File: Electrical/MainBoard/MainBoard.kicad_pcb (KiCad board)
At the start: 4 copper layers, 100 x 100 mm, 152 parts, among them J1 SNAP Program, J10 Refl_Mount, J11 Refl_Mount, J12 Refl_Mount, J13 Refl_PCB_Connect, J14 Refl_PCB_Connect, J15 Refl_PCB_Connect, J16 Conn_02x03_Odd_Even, J17 MEM2061-01-188-00-A, J18 Conn_02x02_Odd_Even, J19 Conn_02x03_Odd_Even, J2 3.3V Supply, J20 Conn_02x03_Odd_Even, J21 Conn_02x03_Odd_Even, J22 Conn_02x02_Odd_Even, J23 Conn_02x03_Odd_Even, J24 Conn_01x04, J3 5V Supply, J4 USB_B_Micro, J5 Battery1, J6 Battery1, J7 GPIO1, J8 Conn_02x04_Odd_Even, J9 USB_B_Micro, K1 QRE1113GR, K2 QRE1113GR, K3 QRE1113GR, M1 Motor_DC, M2 Motor_DC, SW1 Reset, SW10 SW_SPST, SW2 5V Bypass, SW3 All Power Switch, SW4 User_Button, SW5 User_Button, SW6 User_Button, SW7 SW_SPST, SW8 SW_SPST, SW9 SW_SPST, U1 PIC32MZ2048EFH144-I/PL, U10 DRV8842PWPR, U11 Quad_Encoder, U12 Quad_Encoder, U13 DRV8842PWPR, U15 M95M01-DFMN6TP, U2 AP2114HA-3.3TRG1, U3 AP2114HA-3.3TRG1, U4 ICM-42688-P, U5 GSF7002DW, U6 GSF7002DW, U7 GSF7002DW, U8 GSF7002DW, U9 MCP2221A-I_SL

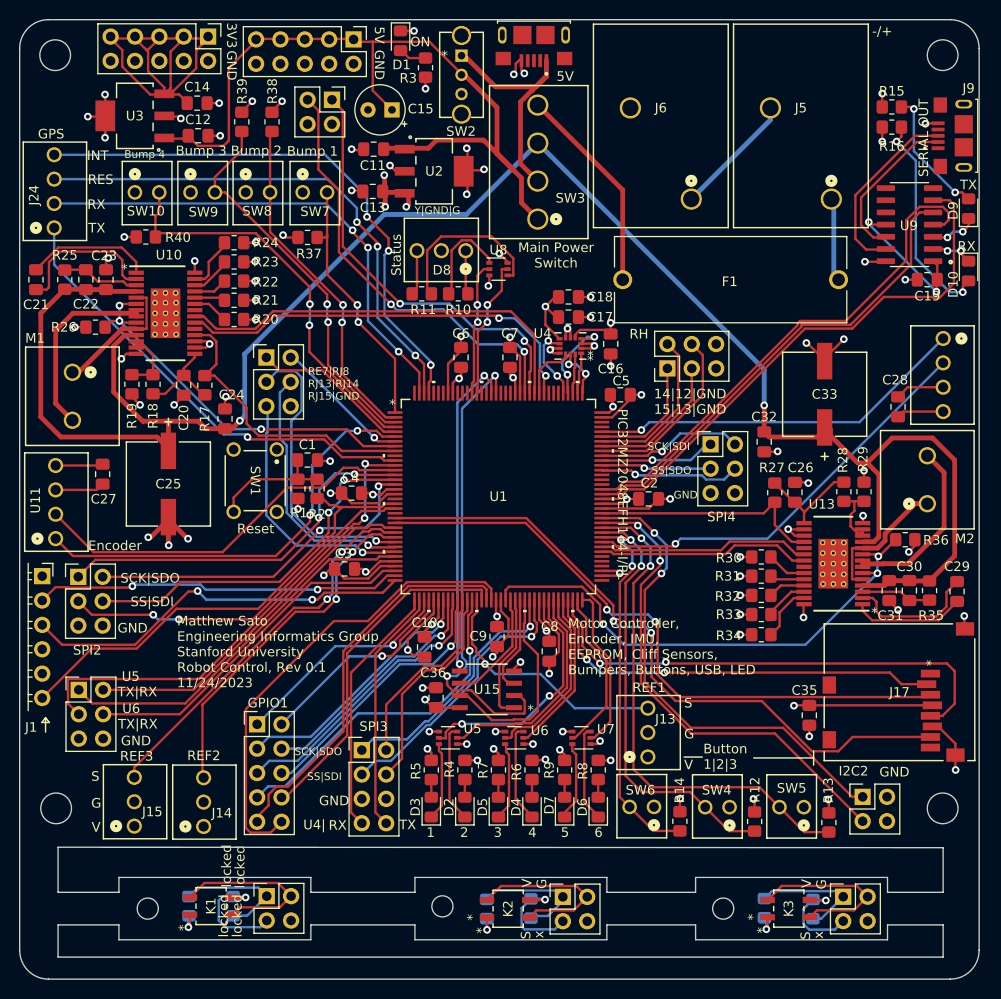
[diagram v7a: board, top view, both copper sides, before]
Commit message: Move reflectlive sensors to own schematic
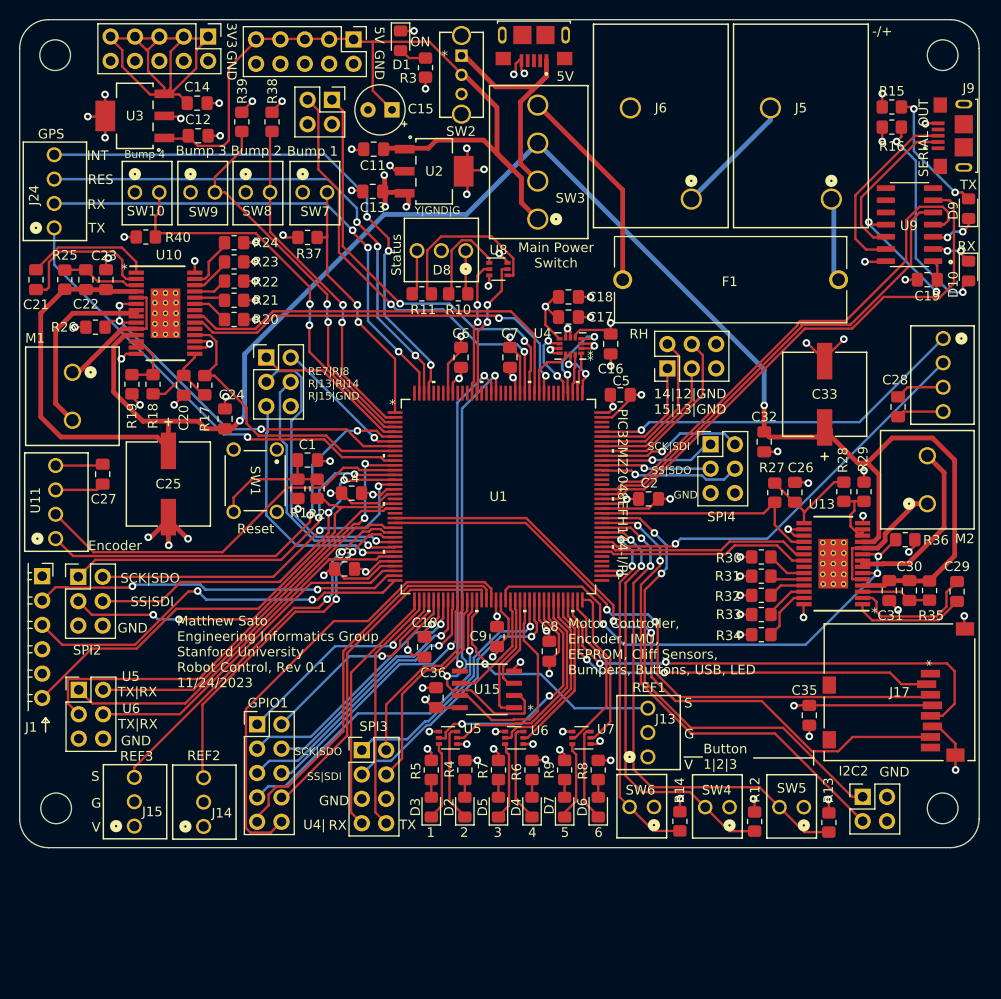
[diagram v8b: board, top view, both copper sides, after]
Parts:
- removed H5, H6, H7: MountingHole, MountingHole:MountingHole_2.2mm_M2
- removed J10, J11, J12: Refl_Mount, Connector_PinHeader_2.54mm:PinHeader_2x02_P2.54mm_Vertical
- removed K1, K2, K3: QRE1113GR, RobotLibrary:ARUSM-313_100CY_FAS-M
- removed R41, R42, R43: 100R, Resistor_SMD:R_0805_2012Metric_Pad1.20x1.40mm_HandSolder
- removed R44, R45, R46: 10k, Resistor_SMD:R_0805_2012Metric_Pad1.20x1.40mm_HandSolder
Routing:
- net Net-(J10-Pin_2): track 18.7 -> 0.00 mm
- net Net-(J11-Pin_2): track 18.4 -> 0.00 mm
- net Net-(J12-Pin_2): track 18.4 -> 0.00 mm
- net Net-(J10-Pin_1): track 13.2 -> 0.00 mm
- net Net-(J12-Pin_1): track 12.9 -> 0.00 mm
- net Net-(J10-Pin_3): track 11.9 -> 0.00 mm, vias 1 -> 0
- net Net-(J11-Pin_1): track 11.4 -> 0.00 mm
- net Net-(J11-Pin_3): track 11.2 -> 0.00 mm, vias 1 -> 0
- net Net-(J12-Pin_3): track 10.8 -> 0.00 mm, vias 1 -> 0
- net Net-(K1-Pad1): track 2.68 -> 0.00 mm, vias 1 -> 0
- net Net-(K3-Pad1): track 2.59 -> 0.00 mm, vias 1 -> 0
- net Net-(K2-Pad1): track 2.48 -> 0.00 mm, vias 1 -> 0
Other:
- board size 100 x 100 mm -> 100 x 86.3 mm
- board text removed: "locked"
- board text removed: "x"
